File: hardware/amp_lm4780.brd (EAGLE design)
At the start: 100 x 100 mm, 77 parts, among them IC2 OPA2333D, Q1 MOSFET-NCHANNEL_SOT23-3, Q2 MOSFET-NCHANNEL_SOT23-3, T1 BC856, X1 2508-5, X2 uC

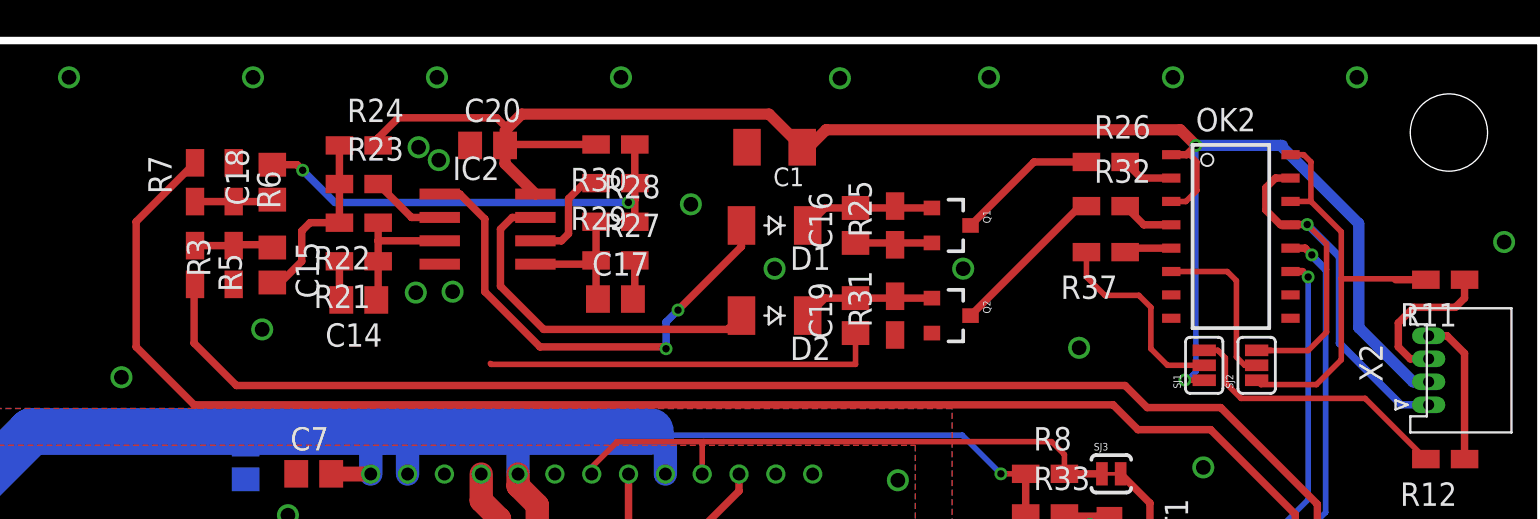
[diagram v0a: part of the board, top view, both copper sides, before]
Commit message: fix gnd_c in amp_lm4780
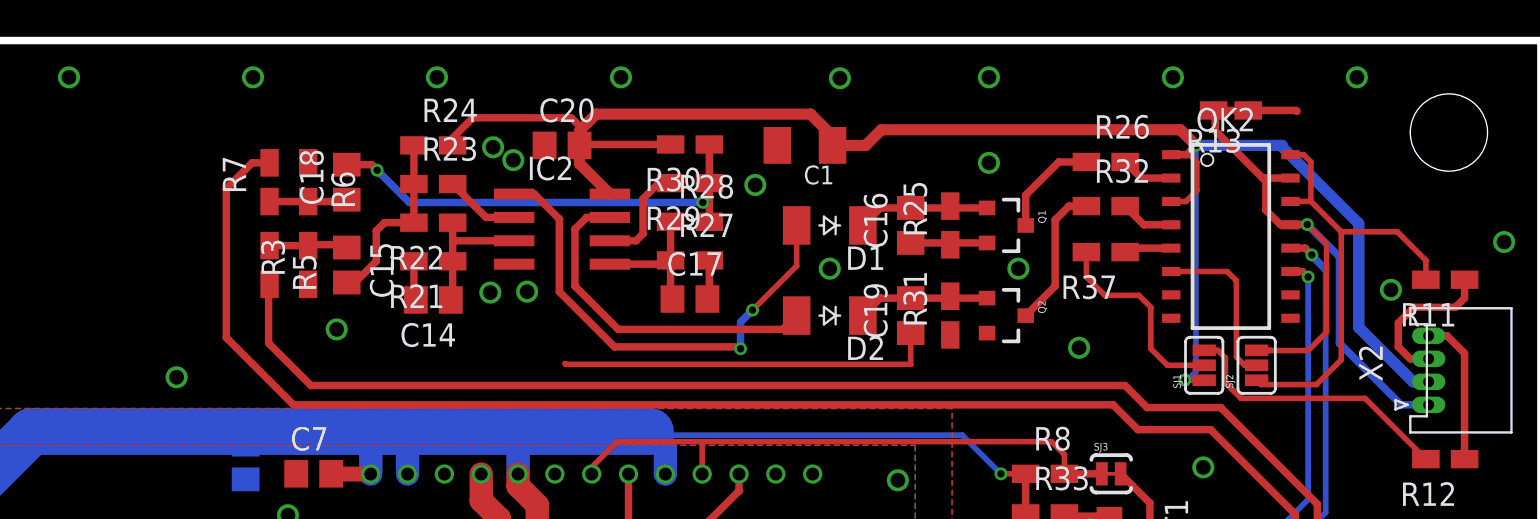
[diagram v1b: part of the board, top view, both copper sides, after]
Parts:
- added R13: 0R_0805, Simplex-Jumpers:R0805W
- IC2: value OPA2333D -> TLC3702
- Q1, Q2: value MOSFET-NCHANNEL_SOT23-3 -> IRLML6246
- moved C15 4.05 mm to (35.1, 87.8)
- moved C18 4.05 mm to (35.1, 92.3)
- moved R3 4.05 mm to (33.0, 87.8)
- moved R6 4.05 mm to (33.0, 92.3)
- moved C14 4.05 mm to (39.8, 85.9)
- moved C17 4.05 mm to (53.8, 86.0)
- moved C20 4.05 mm to (46.8, 94.3)
- moved IC2 4.05 mm to (46.8, 89.8)
- moved R21 4.05 mm to (39.8, 88.0)
- moved R22 4.05 mm to (39.8, 90.1)
- moved R23 4.05 mm to (39.8, 92.2)
- moved R24 4.05 mm to (39.8, 94.3)
- moved R27 4.05 mm to (53.8, 88.0)
- moved R28 4.05 mm to (53.8, 90.2)
- moved R29 4.05 mm to (53.8, 92.2)
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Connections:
- net N$16 renamed NONINV_IN_A
- net N$24 renamed INV_IN_A
- net N$27 renamed OUT_A
- net N$29 renamed NONINV_IN_B
- net N$32 renamed INV_IN_B
- net N$34 renamed OUTB
- net GND_C: now also R13.2
- net GND_I: now also R13.1
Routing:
- net GND_C: track 30.1 -> 35.4 mm
- net N$5: track 106.5 -> 101.5 mm
- net N$7: track 94.9 -> 90.8 mm
- net +3V3D: track 98.8 -> 95.0 mm
- net N$22: track 7.73 -> 5.69 mm
- net SND_DETECT: track 23.7 -> 25.4 mm
- net GND_I: track 42.1 -> 43.7 mm, vias 32 -> 34
- net OUTB: track 19.6 -> 18.6 mm
- net N$36: track 8.76 -> 8.22 mm

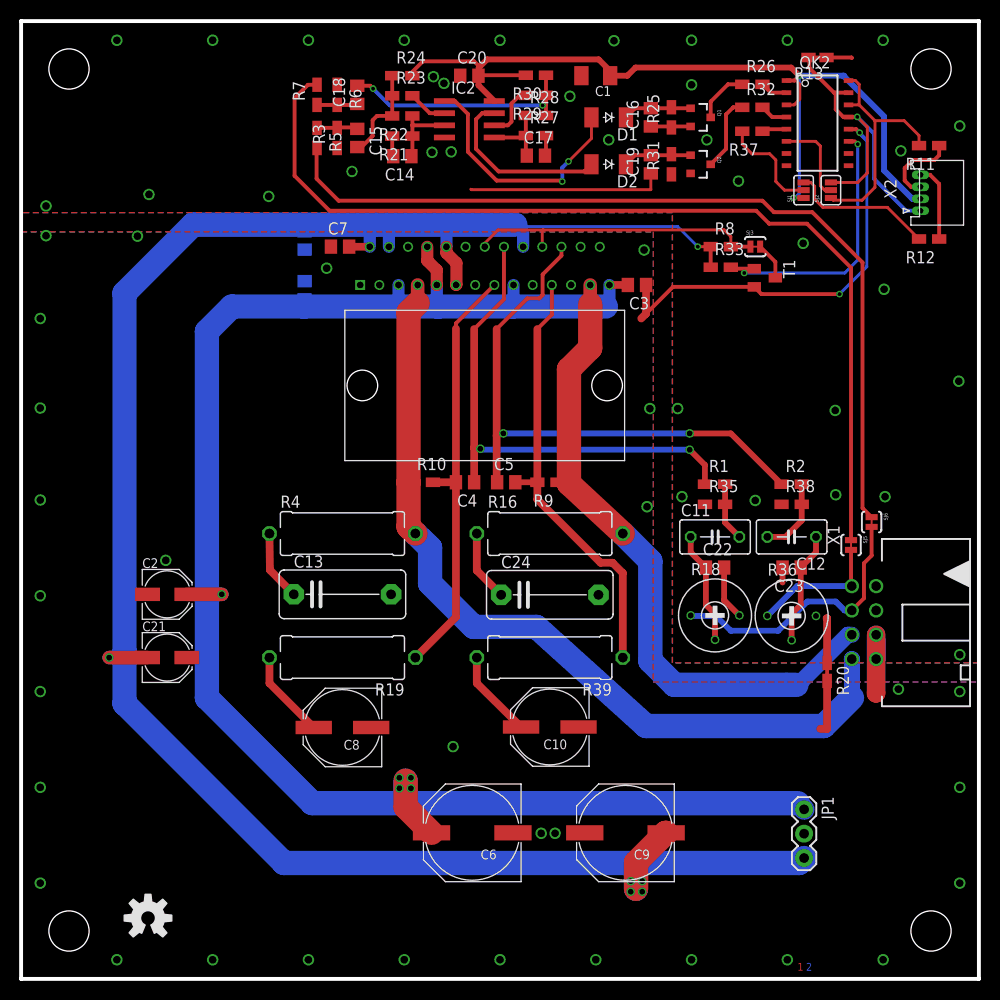
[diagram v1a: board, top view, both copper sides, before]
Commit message: add buffer to snd detect circuit
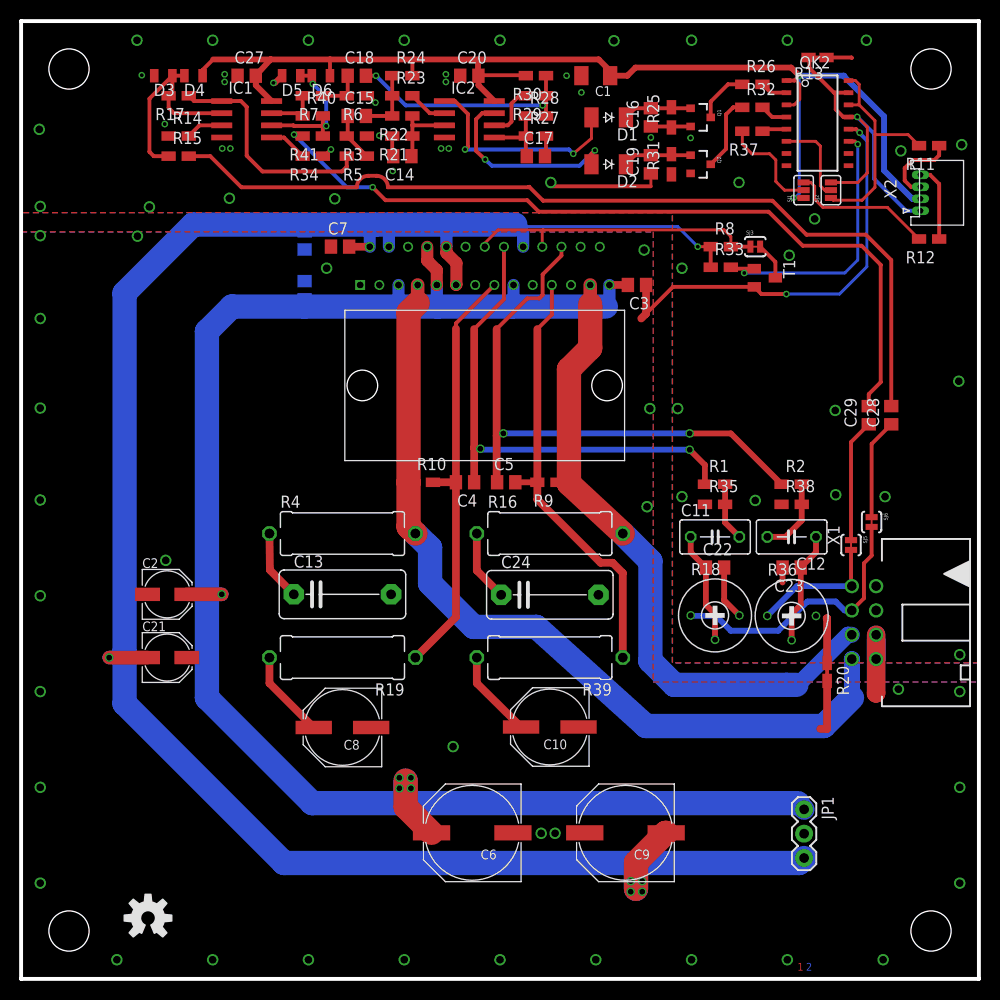
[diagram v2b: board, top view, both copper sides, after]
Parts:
- added C27, C28, C29: 100nF, rcl:C0805
- added D3, D4, D5, D6: BZM55C3V3, diode:MICROMELF-W
- added IC1: OPA2333, linear:SO08
- added R14, R34: 4K7, rcl:R0805W
- added R15, R41: 10K, rcl:R0805W
- added R17, R40: 47K, rcl:R0805W
- moved R5 4.56 mm to (35.0, 85.9), turned to 180 degrees
- moved C15 2.30 mm to (35.0, 90.1), turned to 0 degrees
- moved R3 2.06 mm to (35.0, 88.0), turned to 180 degrees
- moved R6 2.05 mm to (35.0, 92.2), turned to 180 degrees
- moved C18 2.00 mm to (35.0, 94.3), turned to 0 degrees
- moved R7 0.46 mm to (30.4, 92.2), turned to 180 degrees
- moved R28 0.05 mm to (53.8, 90.1)
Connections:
- new net N$11: D3.C, D4.A, IC1.2, R15.1, R17.2
- new net N$12: IC1.5, R34.2
- new net N$13: IC1.7, R40.1, R7.2
- new net N$15: D5.C, D6.A, IC1.6, R40.2, R41.1
- new net N$16: C29.1, SJ5.1
- new net N$17: C29.2, R41.2
- new net N$18: C28.2, R15.2
- new net N$19: C28.1, SJ6.1
- net +3V3D: now also C27.2, D4.C, D6.C, IC1.8
- net GND_I: now also C27.1, D3.A, D5.A, IC1.4, R14.1, R34.1
- net N$5: now also IC1.3, R14.2; no longer R7.2, SJ5.1
- net N$7: now also IC1.1, R17.1; no longer SJ6.1
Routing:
- net N$5: track 101.5 -> 3.91 mm
- net N$18: track 0.00 -> 94.1 mm
- net N$17: track 0.00 -> 83.1 mm, vias 0 -> 2
- net N$7: track 90.8 -> 24.1 mm
- net +3V3D: track 95.0 -> 126.2 mm
- net N$11: track 0.00 -> 21.7 mm
- net N$15: track 0.00 -> 14.9 mm, vias 0 -> 2
- net N$16: track 0.00 -> 12.9 mm
- net N$19: track 0.00 -> 10.5 mm
- net N$13: track 0.00 -> 5.47 mm
- net GND_I: track 43.7 -> 38.5 mm, vias 34 -> 48
- net N$12: track 0.00 -> 4.05 mm
- net N$23: track 10.2 -> 6.95 mm
- net OUT_A: track 26.0 -> 23.0 mm
- net OUTB: track 18.6 -> 20.7 mm, vias 0 -> 2
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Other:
- board text added: "2x30W amplifier circuit rev 3 github.com/rodan/ampy author: petre rodan date: dec 2014"
- board text removed: "2x30W amplifier circuit rev 2 github.com/rodan/ampy author: petre rodan date: dec 2014"

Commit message: redesign snd_detect circuit layout
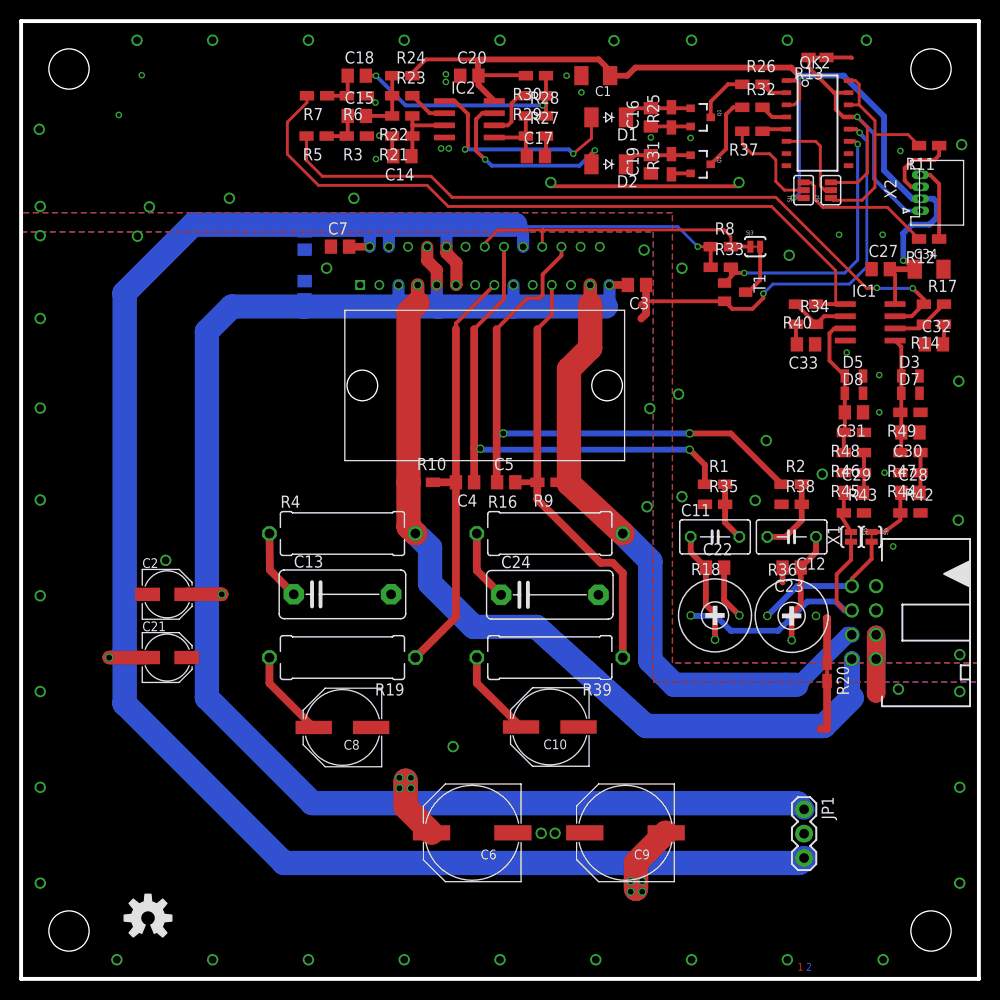
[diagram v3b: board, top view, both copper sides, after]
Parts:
- removed D4, D6: BZM55C3V3, diode:MICROMELF-W
- removed R15, R41: 10K, rcl:R0805W
- added C30, C31: 1nF, rcl:C0805
- added C32, C33: 1uF, rcl:C0805
- added C34: 10uF, rcl:C1206K
- added D7, D8: BZM55C3V3, diode:MICROMELF-W
- added R42, R43: DNP 100K, rcl:R0805W
- added R44, R45: DNP, rcl:R0805W
- added R46, R47: 1K, rcl:R0805W
- added R48, R49: 100K, rcl:R0805W
- C28, C29: value 100nF -> 1uF
- R14, R34: value 4K7 -> 10K
- moved D3 84.1 mm to (92.8, 63.0), turned to 0 degrees
- moved R17 81.8 mm to (95.3, 70.5), turned to 0 degrees
- moved R14 81.3 mm to (95.3, 68.3), turned to 180 degrees
- moved C27 69.2 mm to (89.8, 74.1)
- moved IC1 68.5 mm to (88.7, 68.5)
- moved D5 66.6 mm to (87.0, 63.0), turned to 0 degrees
- moved R40 55.1 mm to (82.0, 70.5), turned to 180 degrees
- moved R34 54.4 mm to (82.0, 68.3), turned to 0 degrees
- moved C28 8.34 mm to (92.8, 50.8), turned to 0 degrees
- moved C29 8.25 mm to (87.0, 50.8), turned to 0 degrees
- moved R5 4.70 mm to (30.9, 88.0)
- moved T1 3.44 mm to (74.5, 71.7)
- moved SJ6 1.55 mm to (88.8, 46.1)
- moved SJ5 0.85 mm to (86.7, 46.1)
- moved R7 0.45 mm to (30.9, 92.2)
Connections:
- removed net N$11: D3.C, D4.A, IC1.2, R15.1, R17.2
- removed net N$15: D5.C, D6.A, IC1.6, R40.2, R41.1
- new net N$20: C32.2, R14.1
- new net N$24: C29.2, R45.1, R46.1
- new net N$27: C31.2, D5.C, D8.C, IC1.3, R46.2, R48.2
- new net N$29: C33.2, R34.1
- net +3V3D: now also C34.1; no longer D4.C, D6.C
- net GND_I: now also C30.1, C31.1, C32.1, C33.1, C34.2, D7.A, D8.A, R42.2, R43.2, R44.2, R45.2, R48.1, R49.1; no longer R14.1, R34.1
- net IN_L: now also SJ5.2; no longer SJ6.2
- net IN_R: now also SJ6.2; no longer SJ5.2
- net N$12: now also IC1.2, R40.2; no longer IC1.5
- net N$13: now also IC1.1; no longer IC1.7
- net N$16: now also C28.1, R42.1, SJ6.1; no longer C29.1, SJ5.1
- net N$17: now also C30.2, D3.C, D7.C, IC1.5, R47.2, R49.2; no longer C29.2, R41.2
- net N$18: now also R44.1, R47.1; no longer R15.2
- net N$19: now also C29.1, R43.1, SJ5.1; no longer C28.1, SJ6.1
- net N$5: now also IC1.6, R17.2; no longer IC1.3
- net N$7: now also IC1.7; no longer IC1.1
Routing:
- net N$18: track 94.1 -> 4.30 mm
- net N$17: track 83.1 -> 12.2 mm, vias 2 -> 0
- net N$13: track 5.47 -> 75.8 mm
- net N$7: track 24.1 -> 77.1 mm, vias 0 -> 2
- net N$11: track 21.7 -> 0.00 mm
- net N$27: track 0.00 -> 15.0 mm
- net N$15: track 14.9 -> 0.00 mm, vias 2 -> 0
- net +3V3D: track 126.2 -> 113.5 mm, vias 2 -> 3
- net GND_I: track 38.5 -> 46.4 mm
- net N$16: track 12.9 -> 6.36 mm
- net N$19: track 10.5 -> 5.05 mm
- net N$24: track 0.00 -> 4.30 mm
- net N$12: track 4.05 -> 6.37 mm
- net N$5: track 3.91 -> 6.15 mm
- net N$29: track 0.00 -> 2.14 mm
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
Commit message: snd_detect cleanup
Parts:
- removed C32, C33: 1uF, rcl:C0805
- removed D7, D8: BZM55C3V3, diode:MICROMELF-W
- removed R42, R43: DNP 100K, rcl:R0805W
- removed R44, R45: DNP, rcl:R0805W
- added D4, D6: 4148, diode:SOD-123_MINI-SMA
- D3, D5: value BZM55C3V3 -> 4148; device diode:MICROMELF-W -> diode:SOD-123_MINI-SMA
- moved D5 7.51 mm to (93.7, 59.6)
- moved C34 5.67 mm to (89.3, 75.7), turned to 180 degrees
- moved C27 5.05 mm to (94.8, 74.0), turned to 180 degrees
- moved C31 2.10 mm to (87.0, 57.0)
- moved R46 2.10 mm to (87.0, 52.9)
- moved R47 2.10 mm to (92.8, 52.9)
- moved R49 2.10 mm to (92.8, 57.0)
- moved C30 2.10 mm to (92.8, 55.0)
- moved R48 2.10 mm to (87.0, 55.0)
- moved T1 1.60 mm to (73.0, 71.7)
- moved IC1 1.30 mm to (88.2, 67.3)
- moved R17 1.30 mm to (94.8, 69.2)
- moved R40 1.30 mm to (81.5, 69.2)
- moved R14 1.30 mm to (94.8, 67.2)
- moved R34 1.30 mm to (81.5, 67.2)
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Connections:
- removed net N$20: C32.2, R14.1
- removed net N$29: C33.2, R34.1
- net GND_I: now also D3.C, D4.C, D6.A, R14.1, R34.1; no longer C32.1, C33.1, D3.A, D7.A, D8.A, R42.2, R43.2, R44.2, R45.2
- net N$16: no longer R42.1
- net N$17: now also D3.A, D5.C; no longer D3.C, D7.C
- net N$18: no longer R44.1
- net N$19: no longer R43.1
- net N$24: no longer R45.1
- net N$27: now also D4.A, D6.C; no longer D5.C, D8.C
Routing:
- net GND_I: track 46.4 -> 49.3 mm, vias 48 -> 49
- net +3V3D: track 113.5 -> 116.1 mm
- net N$17: track 12.2 -> 14.4 mm
- net N$29: track 2.14 -> 0.00 mm
- net N$20: track 2.14 -> 0.00 mm
- net N$24: track 4.30 -> 2.24 mm
- net N$18: track 4.30 -> 2.24 mm
- net N$38: track 29.2 -> 31.1 mm
- net N$13: track 75.8 -> 77.2 mm
- net N$2: track 5.52 -> 6.64 mm
- net N$27: track 15.0 -> 16.0 mm
- net N$19: track 5.05 -> 4.46 mm

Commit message: snd_detect revisited
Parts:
- added C32, C33: 100nF, rcl:C0805
- C14, C17: value 100nF -> 470nF
- D1, D2, D4, D6: value 4148 -> 1N4148
- R22, R28: value 150K -> 47K
- R23, R29: value 100K -> 47K
- R3, R6: value ?K -> 47K
- R5, R7: value ?K -> 1K
- moved R7 23.2 mm to (53.2, 85.9), turned to 0 degrees
- moved C18 18.7 mm to (53.2, 90.1), turned to 180 degrees
- moved R6 18.7 mm to (53.2, 88.0)
- moved C14 9.65 mm to (35.0, 94.3), turned to 0 degrees
- moved C27 7.18 mm to (88.2, 71.3), turned to 0 degrees
- moved R23 6.34 mm to (35.0, 88.0)
- moved R29 6.34 mm to (49.0, 88.0)
- moved C17 6.34 mm to (49.0, 90.1)
- moved R28 5.19 mm to (49.0, 92.2), turned to 180 degrees
- moved R21 5.19 mm to (35.0, 85.9), turned to 0 degrees
- moved R24 5.19 mm to (35.0, 92.2)
- moved R27 5.19 mm to (49.0, 85.9), turned to 180 degrees
- moved C15 4.79 mm to (30.8, 92.2)
- moved R3 4.79 mm to (30.8, 90.1), turned to 0 degrees
- moved C20 4.75 mm to (42.0, 94.3)
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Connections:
- net OUTB renamed N$29
- net OUT_A renamed N$15
- removed net GND_I: C1.2, C14.2, C16.1, C17.2, C19.1, C20.1, C22.2, C23.2, C27.1, C30.1, C31.1, C34.2, D3.C, D4.C, D5.A, D6.A, IC1.4, IC2.4, Q1.2, Q2.2, R13.1, R14.1, R18.3, R20.1, R21.2, R25.1, R27.2, R3.1, R31.1, R34.1, R35.1, R36.3, R38.1, R48.1, R49.1, R6.1, X1.2, X1.4
- removed net INV_IN_A: IC2.2, R23.2
- removed net INV_IN_B: IC2.6, R29.2
- removed net NONINV_IN_A: C14.1, IC2.3, R21.1, R22.1
- removed net NONINV_IN_B: C17.1, IC2.5, R27.1, R28.1
- new net GNDI: C1.2, C14.2, C16.1, C17.2, C19.1, C20.1, C22.2, C23.2, C27.1, C30.1, C31.1, C32.1, C33.1, C34.2, D3.C, D4.C, D5.A, D6.A, IC1.4, IC2.4, Q1.2, Q2.2, R13.1, R14.1, R18.3, R20.1, R21.2, R25.1, R27.2, R3.1, R31.1, R34.1, R35.1, R36.3, R38.1, R48.1, R49.1, R6.1, X1.2, X1.4
- new net N$11: C15.2, R21.1, R22.1, R23.1
- new net N$20: IC2.3, R23.2
- new net N$32: C18.2, R27.1, R28.1, R29.1
- new net N$34: IC2.5, R29.2
- net N$13: now also R5.2; no longer R7.2
- net N$23: now also C14.1, IC2.2; no longer C15.2, R23.1
- net N$26: now also C32.2
- net N$31: now also C17.1, IC2.6; no longer C18.2, R29.1
- net N$33: now also C33.2
- net N$7: now also R7.2; no longer R5.2
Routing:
- net GND_I: track 49.3 -> 0.00 mm, vias 49 -> 0
- net N$7: track 77.0 -> 52.2 mm, vias 2 -> 0
- net GNDI: track 0.00 -> 20.2 mm, vias 0 -> 48
- net N$31: track 24.3 -> 8.06 mm, vias 2 -> 0
- net N$32: track 0.00 -> 8.25 mm
- net NONINV_IN_A: track 7.59 -> 0.00 mm
- net NONINV_IN_B: track 7.58 -> 0.00 mm
- net N$11: track 0.00 -> 7.31 mm
- net N$13: track 77.2 -> 70.8 mm
- net INV_IN_B: track 5.71 -> 0.00 mm
- net N$15: track 23.0 -> 27.5 mm
- net INV_IN_A: track 4.10 -> 0.00 mm
- net N$20: track 0.00 -> 3.81 mm
- net N$34: track 0.00 -> 3.36 mm
- net N$33: track 4.19 -> 7.25 mm
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- added copper zone on layer 1, net GNDI
- added copper zone on layer 16, net GNDI
- removed copper zone on layer 1, net GND_I
- removed copper zone on layer 16, net GND_I
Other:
- board text added: "2x30W amplifier circuit rev 3 github.com/rodan/ampy author: petre rodan date: jan 2015"
- board text removed: "2x30W amplifier circuit rev 3 github.com/rodan/ampy author: petre rodan date: dec 2014"
